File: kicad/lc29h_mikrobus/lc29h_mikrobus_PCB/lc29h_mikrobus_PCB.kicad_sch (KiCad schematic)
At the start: 46 parts, among them IC1 MIKROE-924, IC2 DS28E36BQ+U, IC3 74LVC1G3157GV,125, J1 Conn_Coaxial, J2 Conn_01x03_Pin, Q1 PN2222A, Q2 DMP3013SFV, Q3 BC856B-13-F, Q4 BSS123L, Q5 BSS123L, SW1 SW_Nidec_CAS-120A1, U1 TXS0102DCU, U2 LC29H

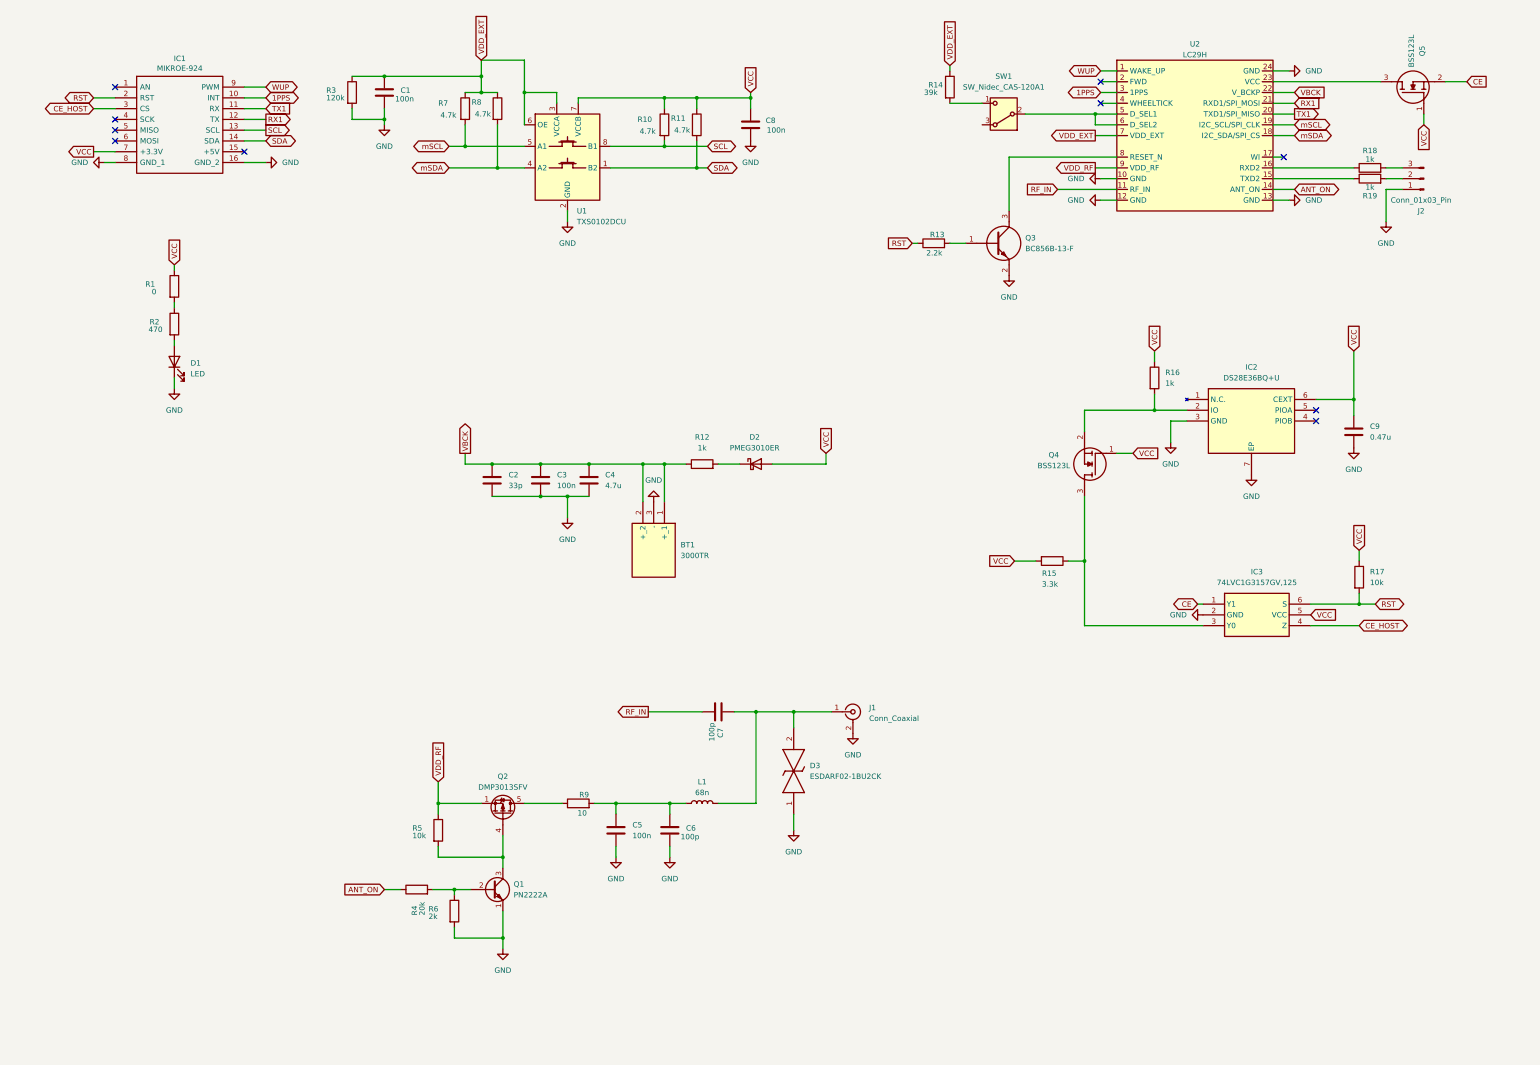
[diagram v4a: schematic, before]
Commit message: BSS123L connections corrected and schematic commented
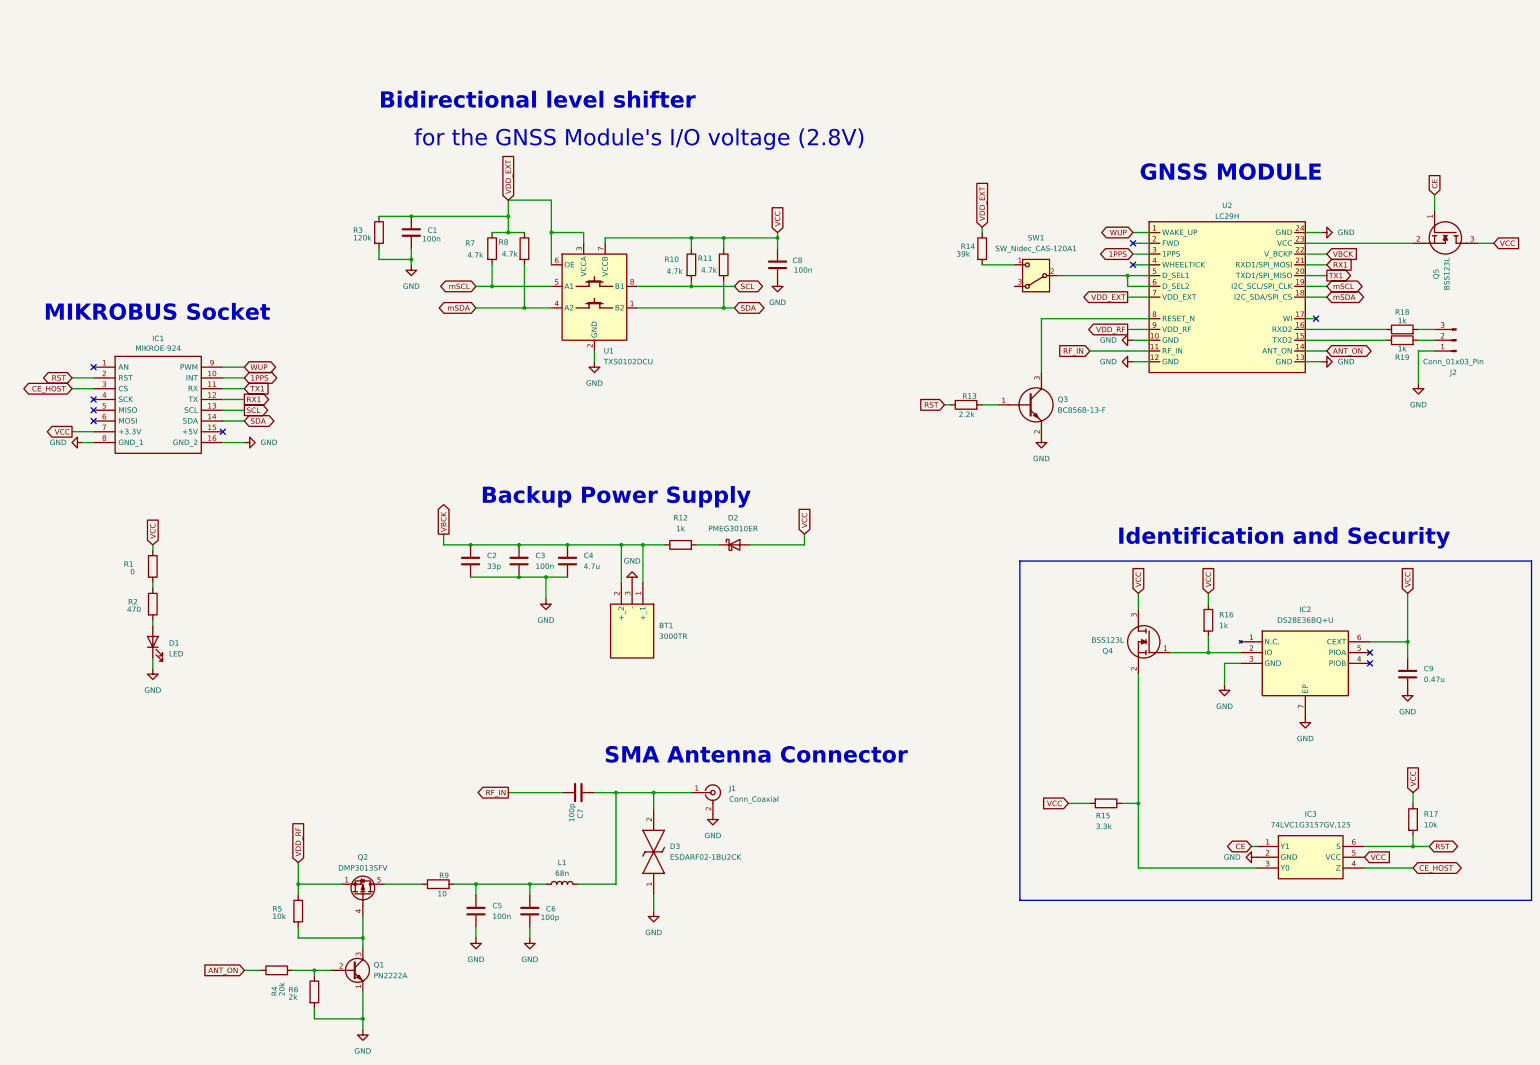
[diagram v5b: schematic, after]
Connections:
- net CE: now also Q5.1 (G); no longer Q5.2 (S)
- net VCC: now also Q4.3 (D), Q5.3 (D); no longer Q4.1 (G), Q5.1 (G)
- net at IC2.2 (IO), R16.2: now also Q4.1 (G); no longer Q4.2 (S)
- net at U2.23 (VCC): now also Q5.2 (S); no longer Q5.3 (D)
- net at IC3.3 (Y0), R15.1: now also Q4.2 (S); no longer Q4.3 (D)
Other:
- note added: "Backup Power Supply"
- note added: "Bidirectional level shifter"
- note added: "GNSS MODULE"
- note added: "Identification and Security"
- note added: "MIKROBUS Socket"
- note added: "SMA Antenna Connector"
- note added: "for the GNSS Module's I/O voltage (2.8V)"
- moved on the sheet: BT1, C1, C2, C3, C4, C5, C6, C7, C8, C9, D1, D2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

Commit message: add power flag and NC to remove errors in schematic ERC
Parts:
- IC1: footprint MIKROE-924:MIKROE924 -> MIKROE924; Description_1 (none) -> microSD click mikroBUS
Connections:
- no-connect marks 10 -> 11

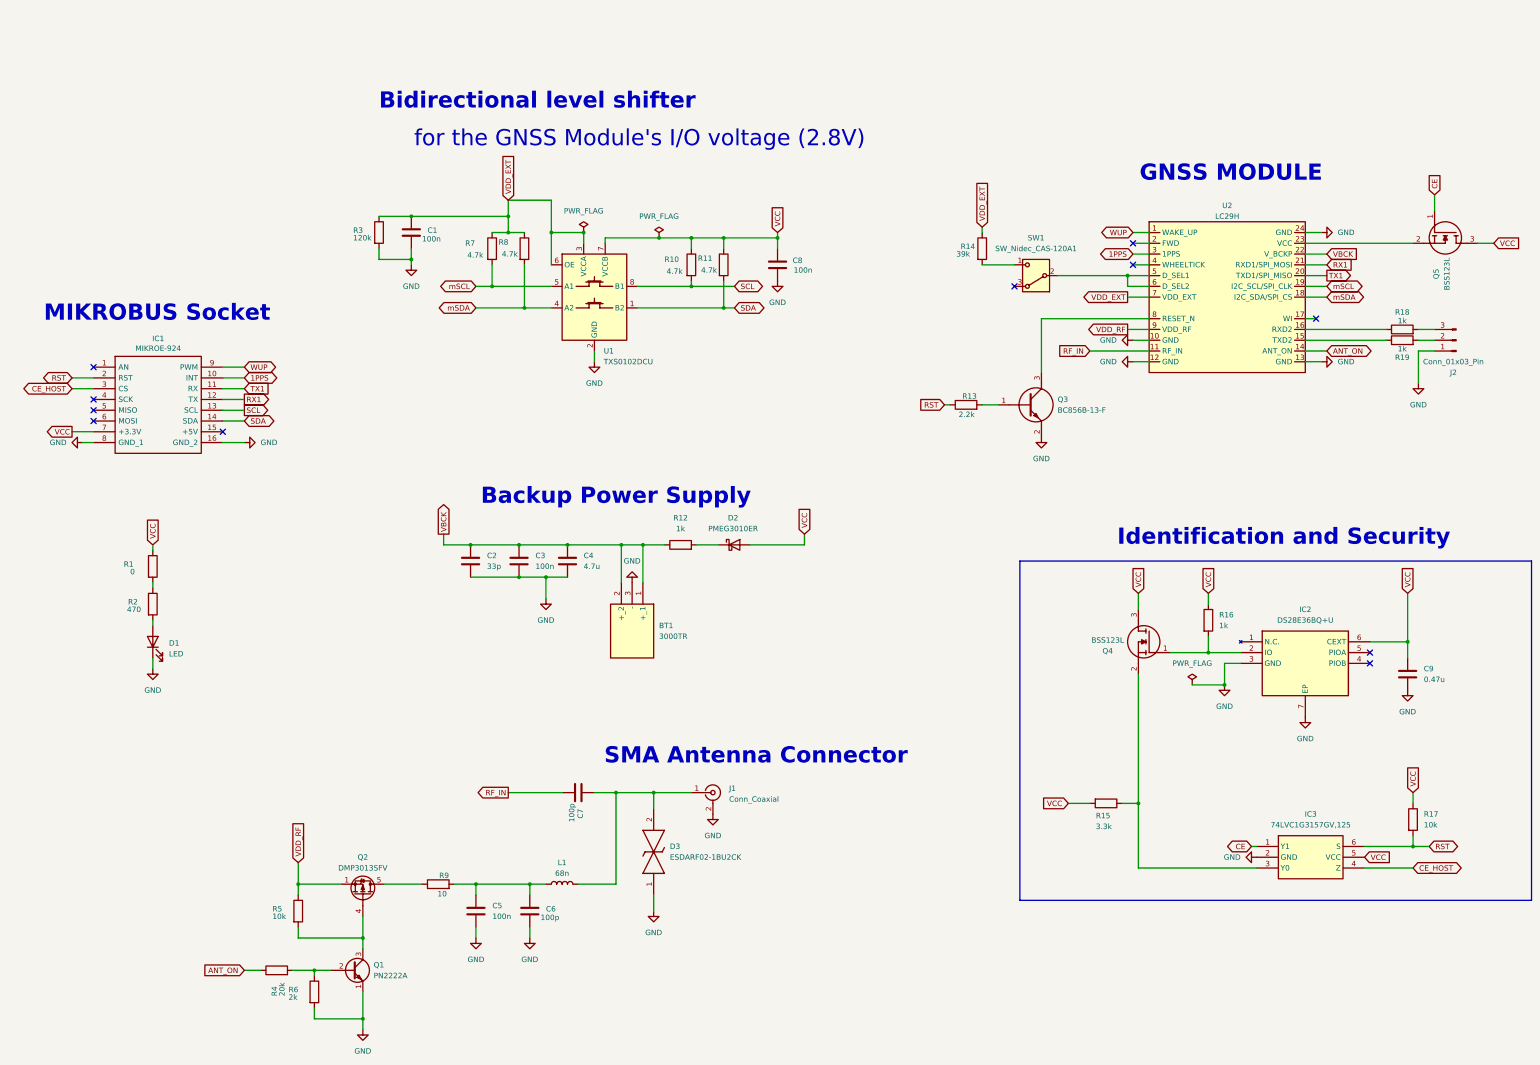
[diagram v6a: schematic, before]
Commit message: 0 ERC errors/warnings after editing symbols
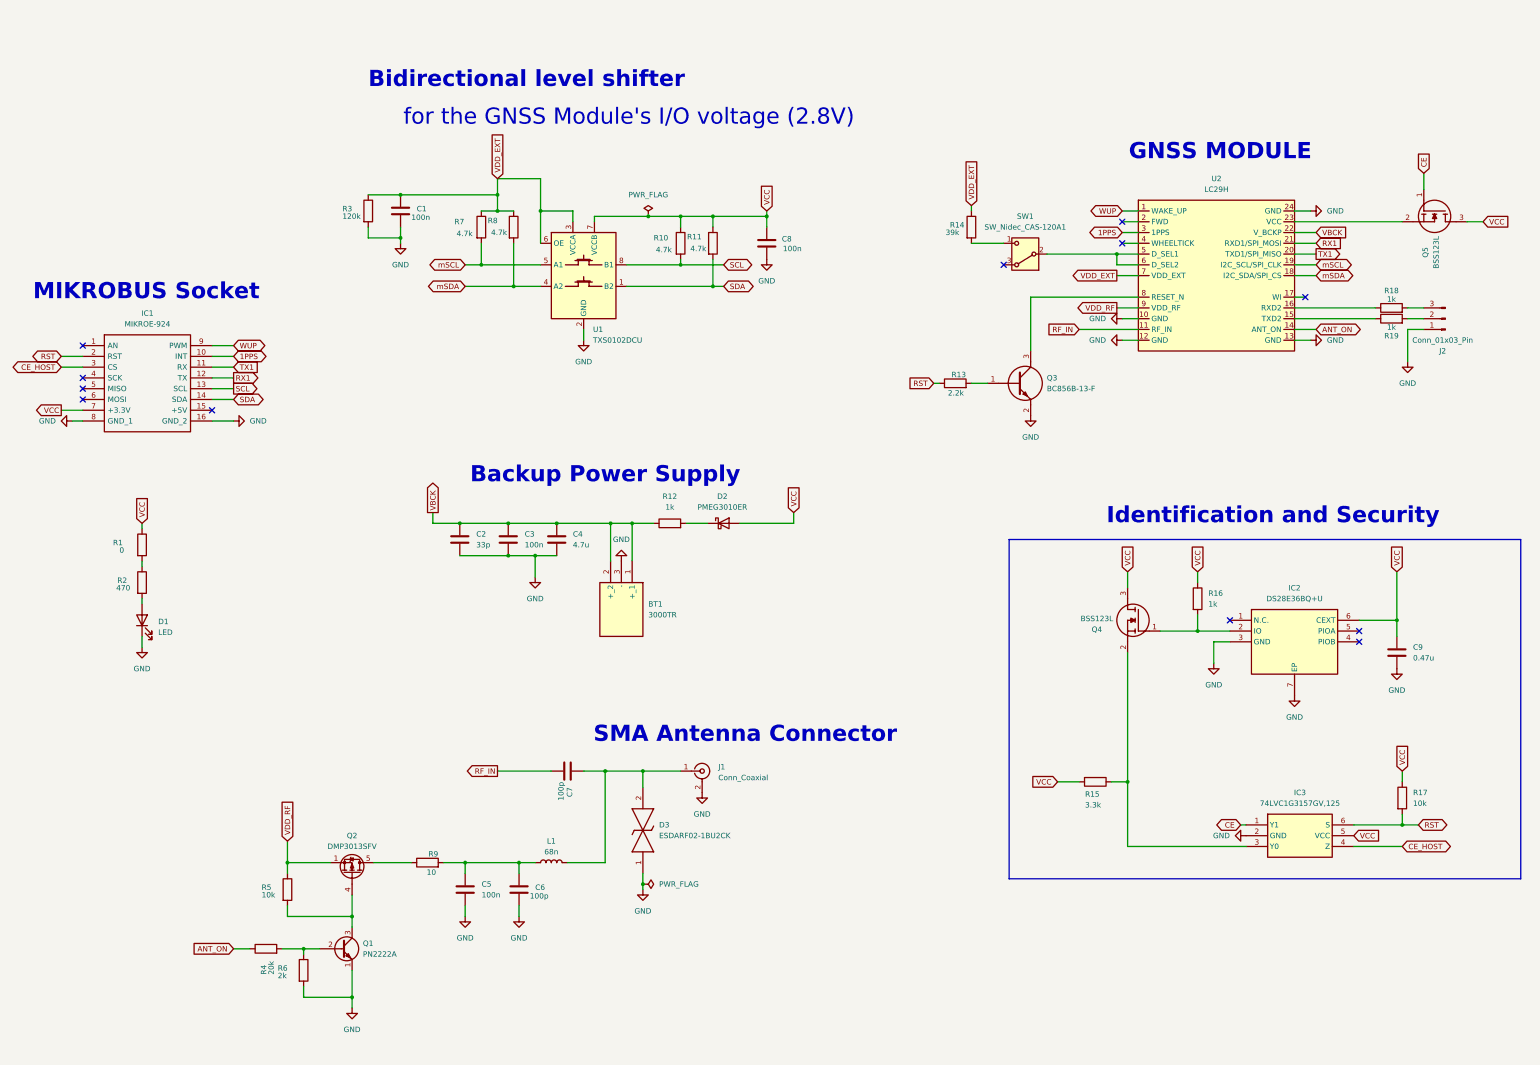
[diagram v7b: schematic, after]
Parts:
- removed IC1: MIKROE-924, MIKROE924, symbol MIKROE-924:MIKROE-924
- removed IC2: DS28E36BQ+U, DS28E36BQ+U:SON95P300X300X80-7N, symbol DS28E36BQ+U:DS28E36BQ+U
- removed U2: LC29H, LC29H:LC29HEA, symbol LC29H:LC29H
- added IC1: MIKROE-924, MIKROE924, symbol NEW_LIB_MIKROE-924:MIKROE-924
- added IC2: DS28E36BQ+U, DS28E36BQ+U:SON95P300X300X80-7N, symbol NEW_LIB_DS28E36BQ+U:DS28E36BQ+U
- added U2: LC29H, LC29H:LC29HEA, symbol NEW_LIB_LC29H:LC29H
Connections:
- net 1PPS: now also IC1.10 (INT), U2.3 (1PPS)
- net ANT_ON: now also U2.14 (ANT_ON)
- net CE_HOST: now also IC1.3 (CS)
- net GND: now also IC1.16 (GND_2), IC1.8 (GND_1), IC2.3 (GND), IC2.7 (EP), U2.10 (GND), U2.12 (GND), U2.13 (GND), U2.24 (GND)
- net RF_IN: now also U2.11 (RF_IN)
- net RST: now also IC1.2 (RST)
- net RX1: now also IC1.12 (TX), U2.21 (RXD1/SPI_MOSI)
- net SCL: now also IC1.13 (SCL)
- net SDA: now also IC1.14 (SDA)
- net TX1: now also IC1.11 (RX), U2.20 (TXD1/SPI_MISO)
- net VBCK: now also U2.22 (V_BCKP)
- net VCC: now also IC1.7 (+3.3V), IC2.6 (CEXT)
- net VDD_EXT: now also U2.7 (VDD_EXT)
- net VDD_RF: now also U2.9 (VDD_RF)
- net WUP: now also IC1.9 (PWM), U2.1 (WAKE_UP)
- net mSCL: now also U2.19 (I2C_SCL/SPI_CLK)
- net mSDA: now also U2.18 (I2C_SDA/SPI_CS)
- net at SW1.2 (B): now also U2.5 (D_SEL1), U2.6 (D_SEL2)
- net at R19.1: now also U2.15 (TXD2)
- net at Q4.1 (G), R16.2: now also IC2.2 (IO)
- net at Q5.2 (S): now also U2.23 (VCC)
- net at Q3.3 (C): now also U2.8 (RESET_N)
- net at R18.1: now also U2.16 (RXD2)
- no-connect marks 11 -> 12
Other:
- moved on the sheet: BT1, C1, C2, C3, C4, C5, C6, C7, C8, C9, D1, D2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

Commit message: replace all 201 SMD components with 805 for hand soldering
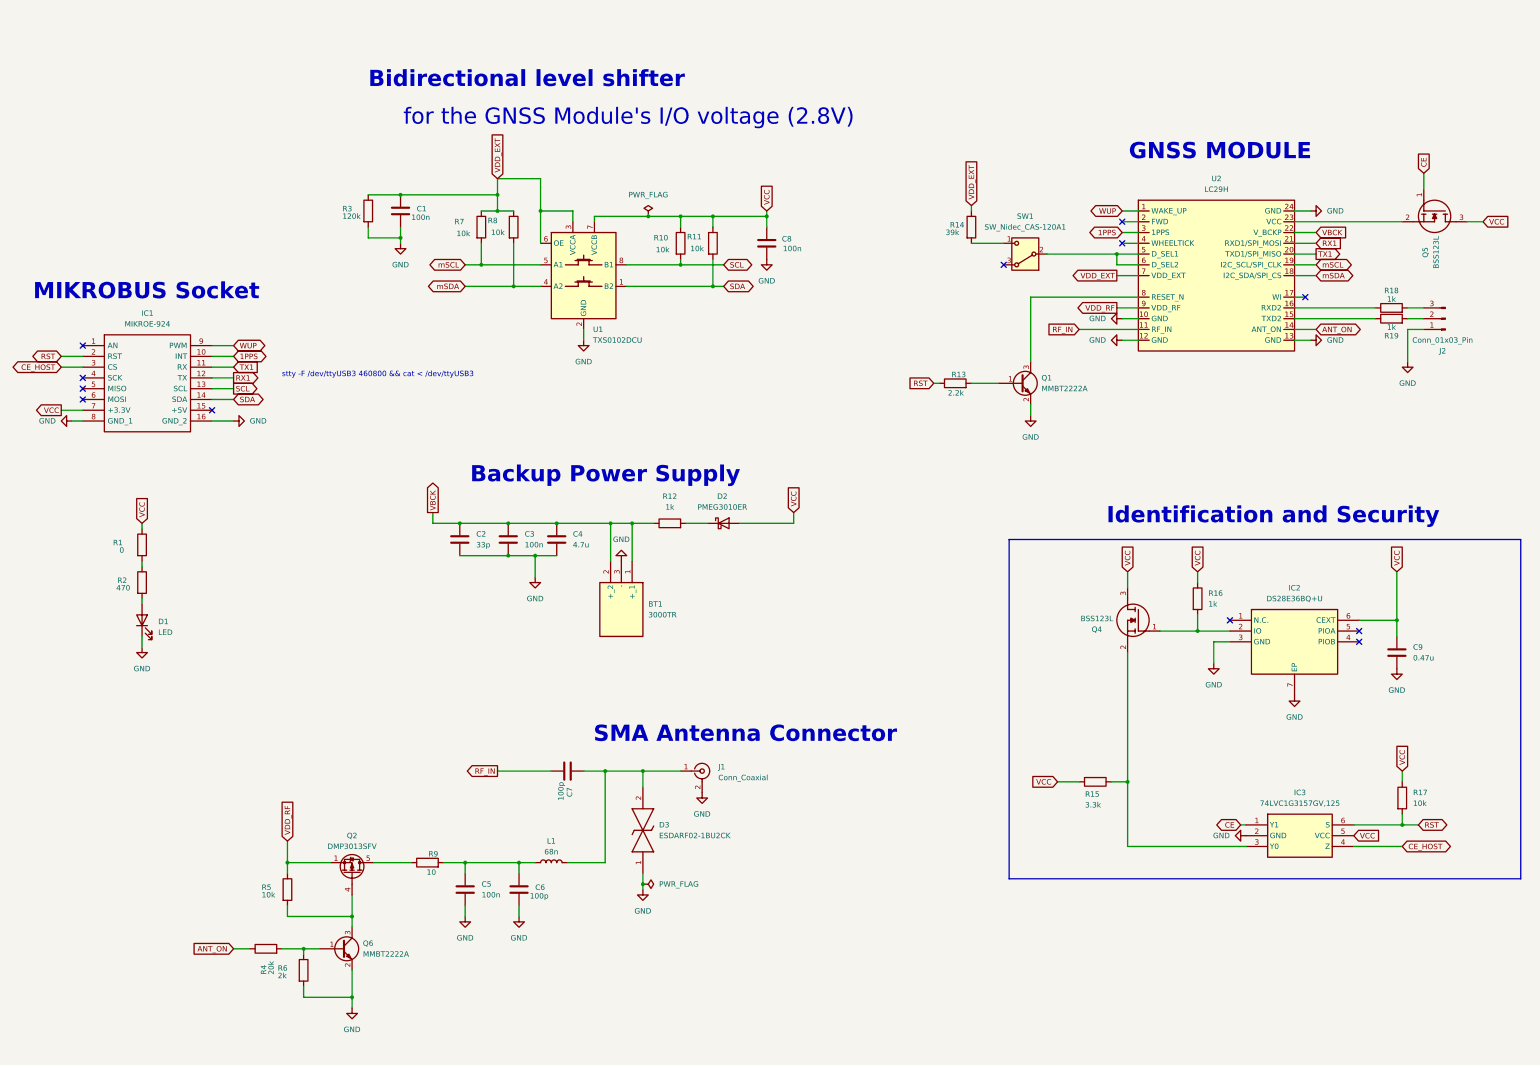
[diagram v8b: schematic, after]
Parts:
- removed Q1: PN2222A, Package_TO_SOT_THT:TO-92_Inline, symbol Transistor_BJT:PN2222A
- removed Q3: BC856B-13-F, BC856B-13-F:SOT96P240X110-3N, symbol BC856B-13-F:BC856B-13-F
- added Q1, Q6: MMBT2222A, Package_TO_SOT_SMD:SOT-23, symbol Transistor_BJT:MMBT2222A
- C1, C2, C3, C4, C5, C6, C7, C8, C9: footprint Capacitor_SMD:C_0201_0603Metric -> Capacitor_SMD:C_0805_2012Metric_Pad1.18x1.45mm_HandSolder
- IC1: footprint MIKROE924 -> MIKROE-924:MIKROE924
- L1: footprint Inductor_SMD:L_0201_0603Metric -> Inductor_SMD:L_0805_2012Metric_Pad1.05x1.20mm_HandSolder
- R10, R11, R7, R8: value 4.7k -> 10k; footprint Resistor_SMD:R_0201_0603Metric -> Resistor_SMD:R_0805_2012Metric_Pad1.20x1.40mm_HandSolder
- R12, R13, R14, R15, R16, R17, R18, R19, R2, R3, R4, R5, R6, R9: footprint Resistor_SMD:R_0201_0603Metric -> Resistor_SMD:R_0805_2012Metric_Pad1.20x1.40mm_HandSolder
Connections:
- net GND: now also Q1.2 (E), Q6.2 (E)
- net at Q2.4 (G), R5.2: now also Q6.3 (C)
- net at R4.2, R6.1: now also Q6.1 (B)
- net at U2.8 (RESET_N): now also Q1.3 (C)
- net at R13.2: now also Q1.1 (B)
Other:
- note added: "stty -F /dev/ttyUSB3 460800 && cat < /dev/ttyUSB3"
